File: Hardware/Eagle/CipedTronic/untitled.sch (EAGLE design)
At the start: 14 parts, among them IC1 ATMEGA48/88/168-PU, T1 BC547

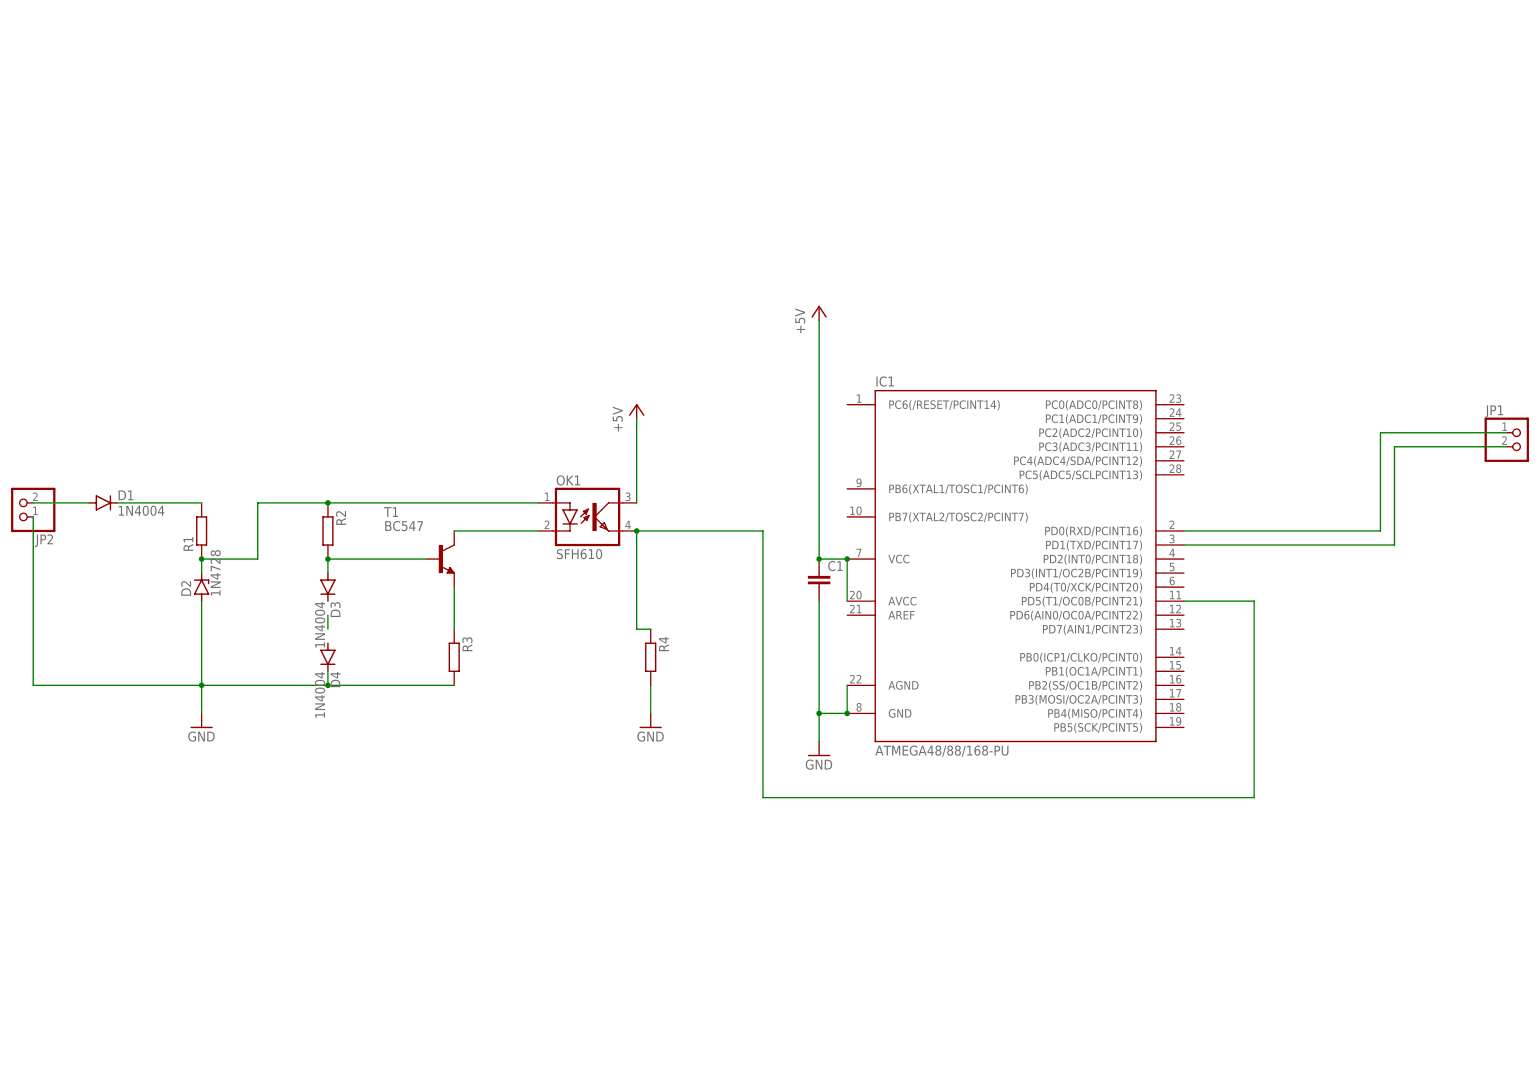
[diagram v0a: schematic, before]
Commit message: migration to seed xaio esp32
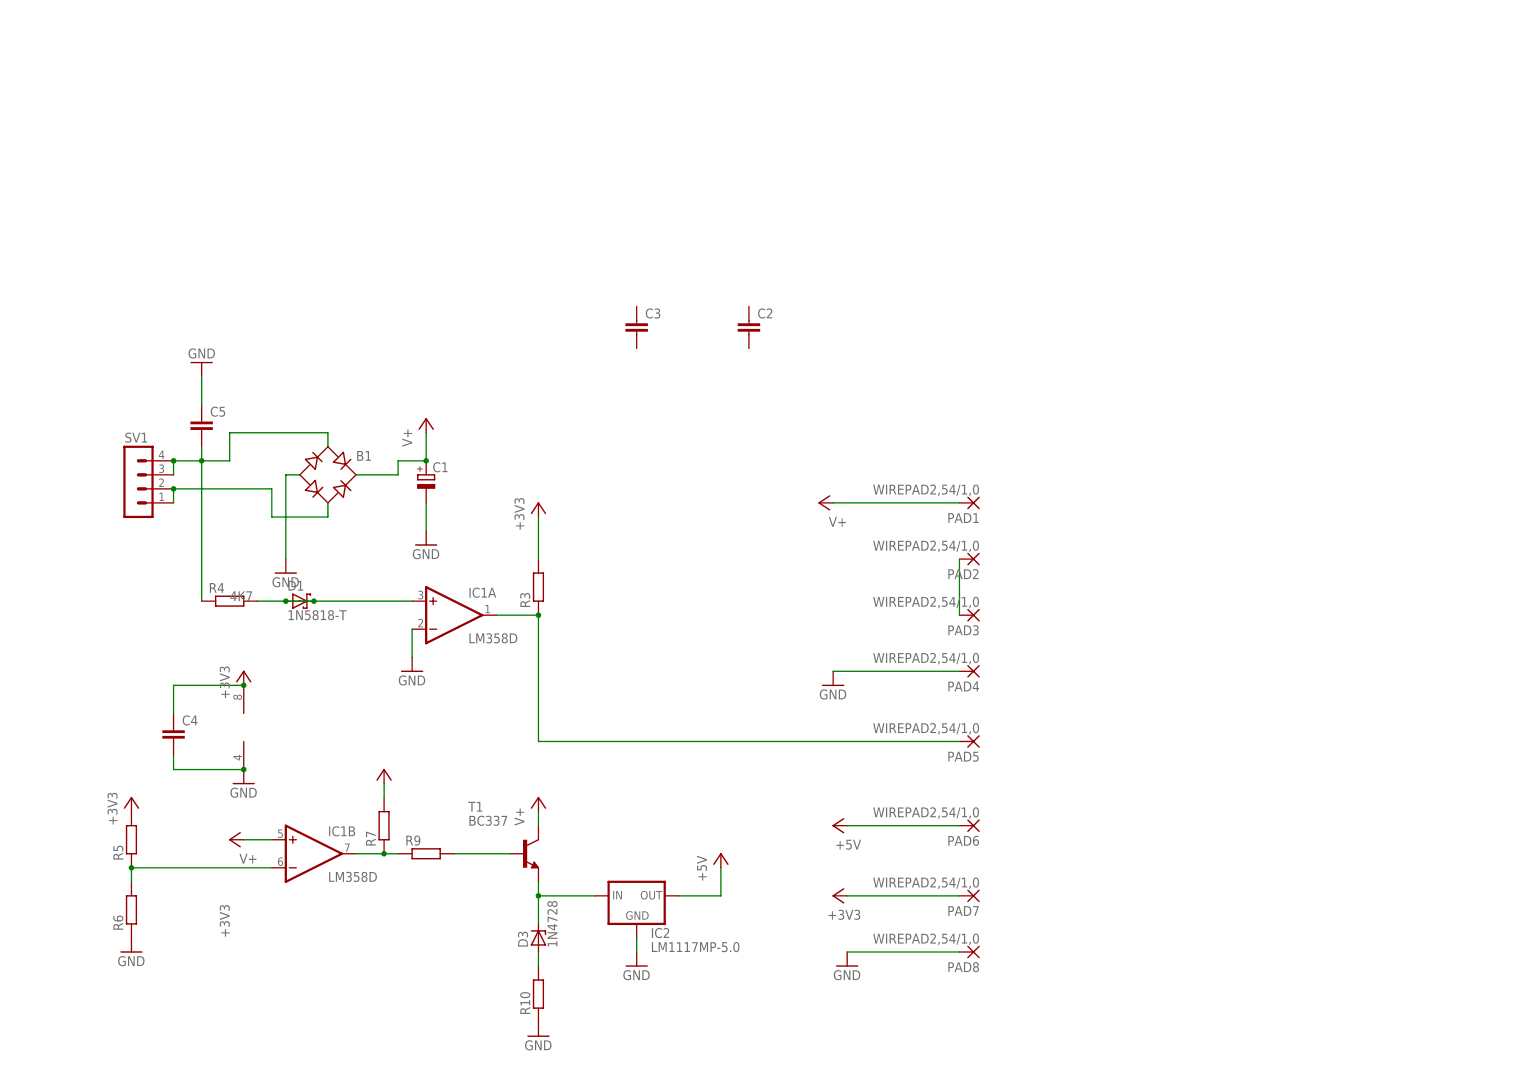
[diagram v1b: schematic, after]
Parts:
- removed D2: 1N4728, diode:1N4728
- removed D4: 1N4004, diode:1N4004
- removed JP1, JP2: (no value), pinhead:PINHD-1X2
- removed OK1: SFH610, optocoupler:SFH610
- removed R1, R2: (no value), rcl:R-EU_0204/7
- added B1: (no value), rectifier:B-DIL
- added C2, C3, C4, C5: (no value), rcl:C-EU050-024X044
- added IC2: LM1117MP-5.0, lm1117_11:LM1117MP-5.0
- added PAD1, PAD2, PAD3, PAD4, PAD5, PAD6, PAD7, PAD8: WIREPAD2,54/1,0, wirepad:WIREPAD2,54/1,0
- added R10, R5, R6, R7, R9: (no value), rcl:R-EU_0204/2V
- added SV1: (no value), con-lstb:MA04-1
- C1: device rcl:C-EU025-024X044 -> rcl:CPOL-EUTT5D11
- D1: value 1N4004 -> 1N5818-T; device diode:1N4004 -> diode:1N5818-T
- D3: value 1N4004 -> 1N4728; device diode:1N4004 -> diode:1N4728
- IC1: value ATMEGA48/88/168-PU -> LM358D; device atmega8:ATMEGA48/88/168-PU -> linear:LM358D
- R3: device rcl:R-EU_0204/7 -> rcl:R-EU_0204/2V
- R4: device rcl:R-EU_0204/7 -> rcl:R-EU_0204/2V; SPICEPREFIX (none) -> 4K7
- T1: value BC547 -> BC337; device transistor:BC547 -> transistor:BC337
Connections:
- removed net N$6: IC1.PD0(RXD/PCINT16), JP1.1
- removed net N$7: OK1.C, T1.C
- new net +3V3: B1.+, C1.+, C4.1, IC1P.V+, PAD7.P, R3.2, R5.2, R7.2
- new net N$11: IC1B.-IN, R5.1, R6.2
- new net N$12: PAD2.P, PAD3.P
- new net N$4: R9.2, T1.B
- new net V+: IC1B.+IN, PAD1.P, T1.C
- net +5V: now also IC2.OUT, PAD6.P; no longer C1.1, IC1.AVCC, IC1.VCC@1, OK1.COL
- net GND: now also B1.-, C1.-, C4.2, C5.1, IC1A.-IN, IC1P.V-, IC2.GND, PAD4.P, PAD8.P, R10.1, R6.1; no longer C1.2, D2.A, D4.C, IC1.AGND, IC1.GND@1, JP2.1, R3.2, R4.2
- net N$1: now also B1.AC1, C5.2, R4.1, SV1.3, SV1.4; no longer D1.C, R1.2
- net N$10: now also D3.A, R10.2; no longer IC1.PD1(TXD/PCINT17), JP1.2
- net N$2: now also B1.AC2, SV1.1, SV1.2; no longer R3.1, T1.E
- net N$3: now also IC1A.OUT, PAD5.P, R3.1; no longer D3.A, R2.2, T1.B
- net N$5: now also D1.A, D1.C, IC1A.+IN, R4.2; no longer D2.C, OK1.A, R1.1, R2.1
- net N$8: now also IC1B.OUT, R7.1, R9.1; no longer D1.A, JP2.2
- net N$9: now also D3.C, IC2.IN, T1.E; no longer IC1.PD5(T1/OC0B/PCINT21), OK1.EMIT, R4.1
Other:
- moved on the sheet: D3, R3, R4, T1

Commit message: Cipedtronic with esp32
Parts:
- added D2: 1N4728, diode:1N4728
- added D4, D5: 1N5818-T, diode:1N5818-T
- added R1, R8: 10k, rcl:R-EU_0204/2V
- added R2: 1m, rcl:R-EU_0204/2V
- C2: value (none) -> 0,1uf
- C3: value (none) -> 0.33uf
- R3: value (none) -> 10k
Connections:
- net N$2 renamed V-
- new net N$6: IC1A.+IN, R1.1, R2.2
- new net N$7: D4.A, D4.C, D5.A, IC1A.-IN, R3.2
- net +3V3: now also R3.1, R8.1; no longer R3.2
- net +5V: now also C2.1
- net GND: now also C2.2, C3.2, D2.A, D5.C; no longer IC1A.-IN
- net N$3: now also R2.1, R8.2; no longer R3.1
- net N$5: now also D2.C, R1.2; no longer IC1A.+IN
- net N$9: now also C3.1
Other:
- moved on the sheet: C2, C3, R3

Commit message: Rename sketch Extend Timer Add namespace
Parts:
- removed C1: (no value), rcl:CPOL-EUTT5D11
- removed D3: 1N4728, diode:1N4728
- removed R10, R9: (no value), rcl:R-EU_0204/2V
- removed T1: BC337, transistor:BC337
- added PAD10, PAD9: Light on/off switch, wirepad:2,15/1,0
- added Q1, Q3: FDD4141TO252, transistor-fet:FDD4141TO252
- PAD1: value WIREPAD2,54/1,0 -> Light on/off ESP32; device wirepad:WIREPAD2,54/1,0 -> wirepad:2,15/1,0
- PAD2: value WIREPAD2,54/1,0 -> 5V ESP32; device wirepad:WIREPAD2,54/1,0 -> wirepad:2,15/1,0
- PAD3: value WIREPAD2,54/1,0 -> 3.3V ESP32; device wirepad:WIREPAD2,54/1,0 -> wirepad:2,15/1,0
- PAD4, PAD5: value WIREPAD2,54/1,0 -> LED; device wirepad:WIREPAD2,54/1,0 -> wirepad:2,15/1,0
- PAD6: value WIREPAD2,54/1,0 -> Pulses ESP32; device wirepad:WIREPAD2,54/1,0 -> wirepad:2,15/1,0
- PAD7, PAD8: value WIREPAD2,54/1,0 -> Super Cap; device wirepad:WIREPAD2,54/1,0 -> wirepad:2,15/1,0
- R5: value (none) -> 10k; device rcl:R-EU_0204/2V -> rcl:R-EU_MELF0204W
- R6, R7: value (none) -> 10k
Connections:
- removed net N$10: D3.A, R10.2
- removed net N$11: IC1B.-IN, R5.1, R6.2
- removed net N$12: PAD2.P, PAD3.P
- new net N$13: D1.A, R4.2
- new net N$2: PAD4.P, Q3.D
- net +3V3: now also PAD10.P, PAD2.P; no longer C1.+, R5.2, R7.2
- net +5V: now also PAD3.P; no longer PAD6.P
- net GND: now also PAD5.P, R5.2, R7.2; no longer C1.-, PAD4.P, R10.1, R6.1
- net N$3: now also PAD6.P; no longer PAD5.P
- net N$4: now also C3.1, IC2.IN, Q1.D; no longer R9.2, T1.B
- net N$5: no longer D1.A, R4.2
- net N$8: now also PAD1.P, PAD9.P, Q3.G; no longer IC1B.OUT, R9.1
- net N$9: now also Q1.G, R5.1, R6.2; no longer C3.1, D3.C, IC2.IN, T1.E
- net V+: now also Q1.S, Q3.S, R6.1; no longer IC1B.+IN, PAD1.P, T1.C
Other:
- note added: "10K"
- note added: "3.3 V"
- note added: "Reference 1 Volt"
- note added: "Should switch >= 5Volts"
- moved on the sheet: C2, C3, C4, D1, D2, D4, D5, IC1A, IC2, R1, R2, R3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

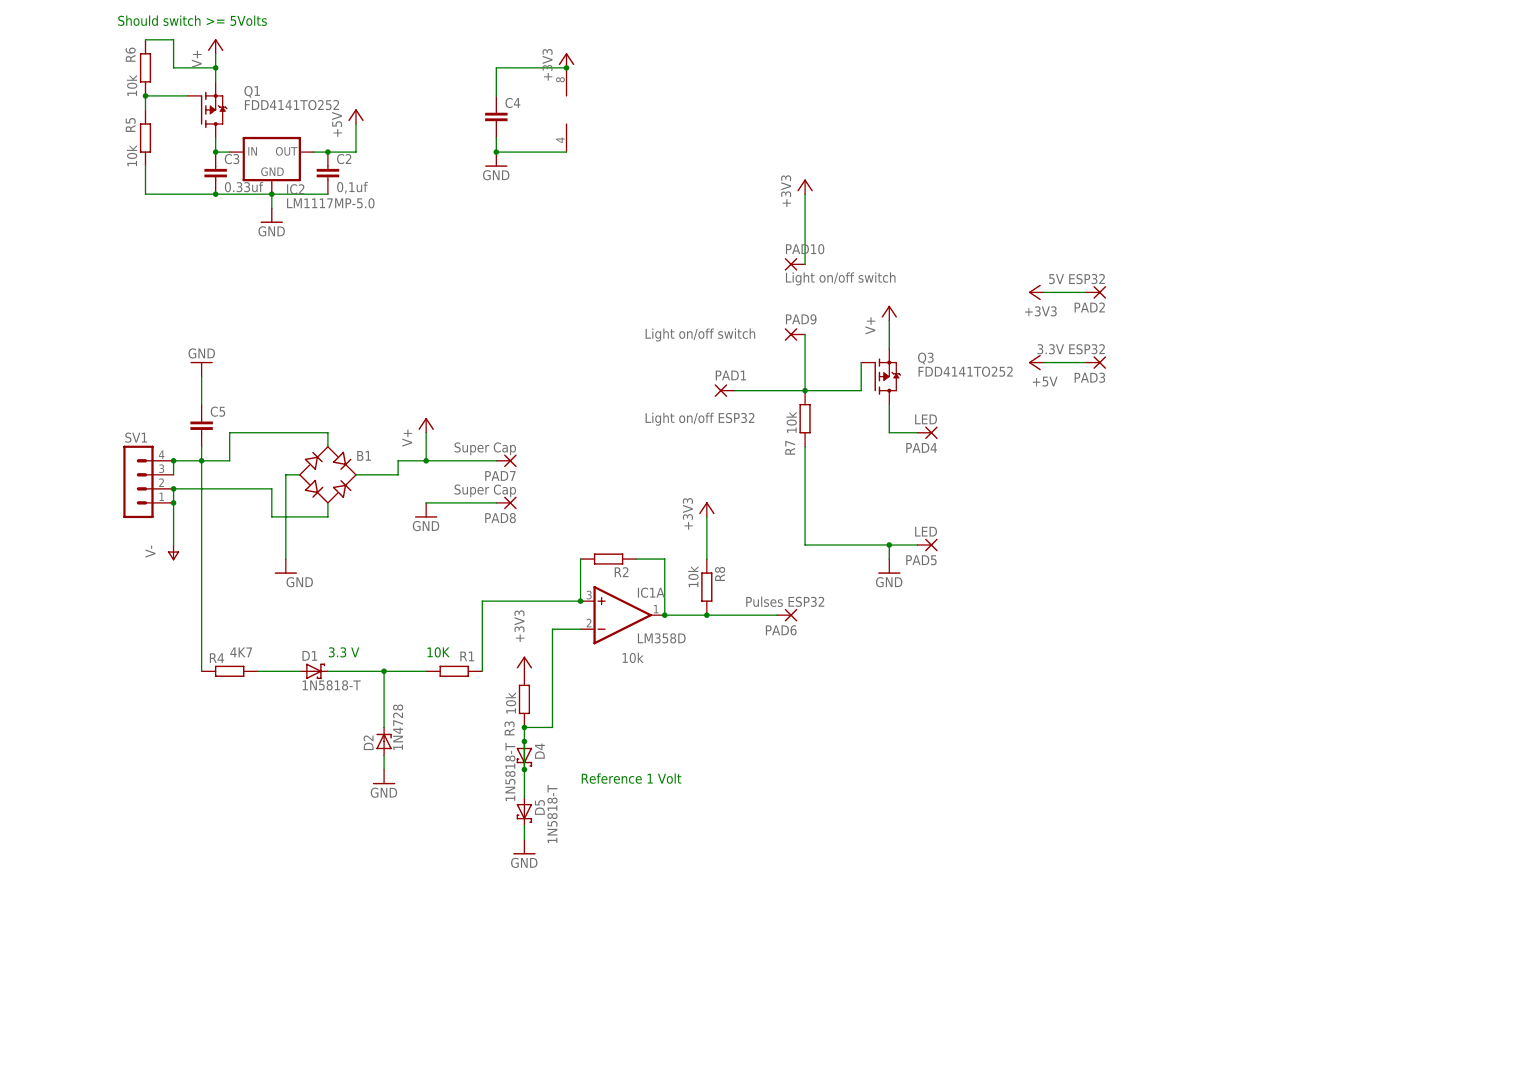
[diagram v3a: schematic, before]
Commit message: battery load functions distance sensor improved pulse formatting
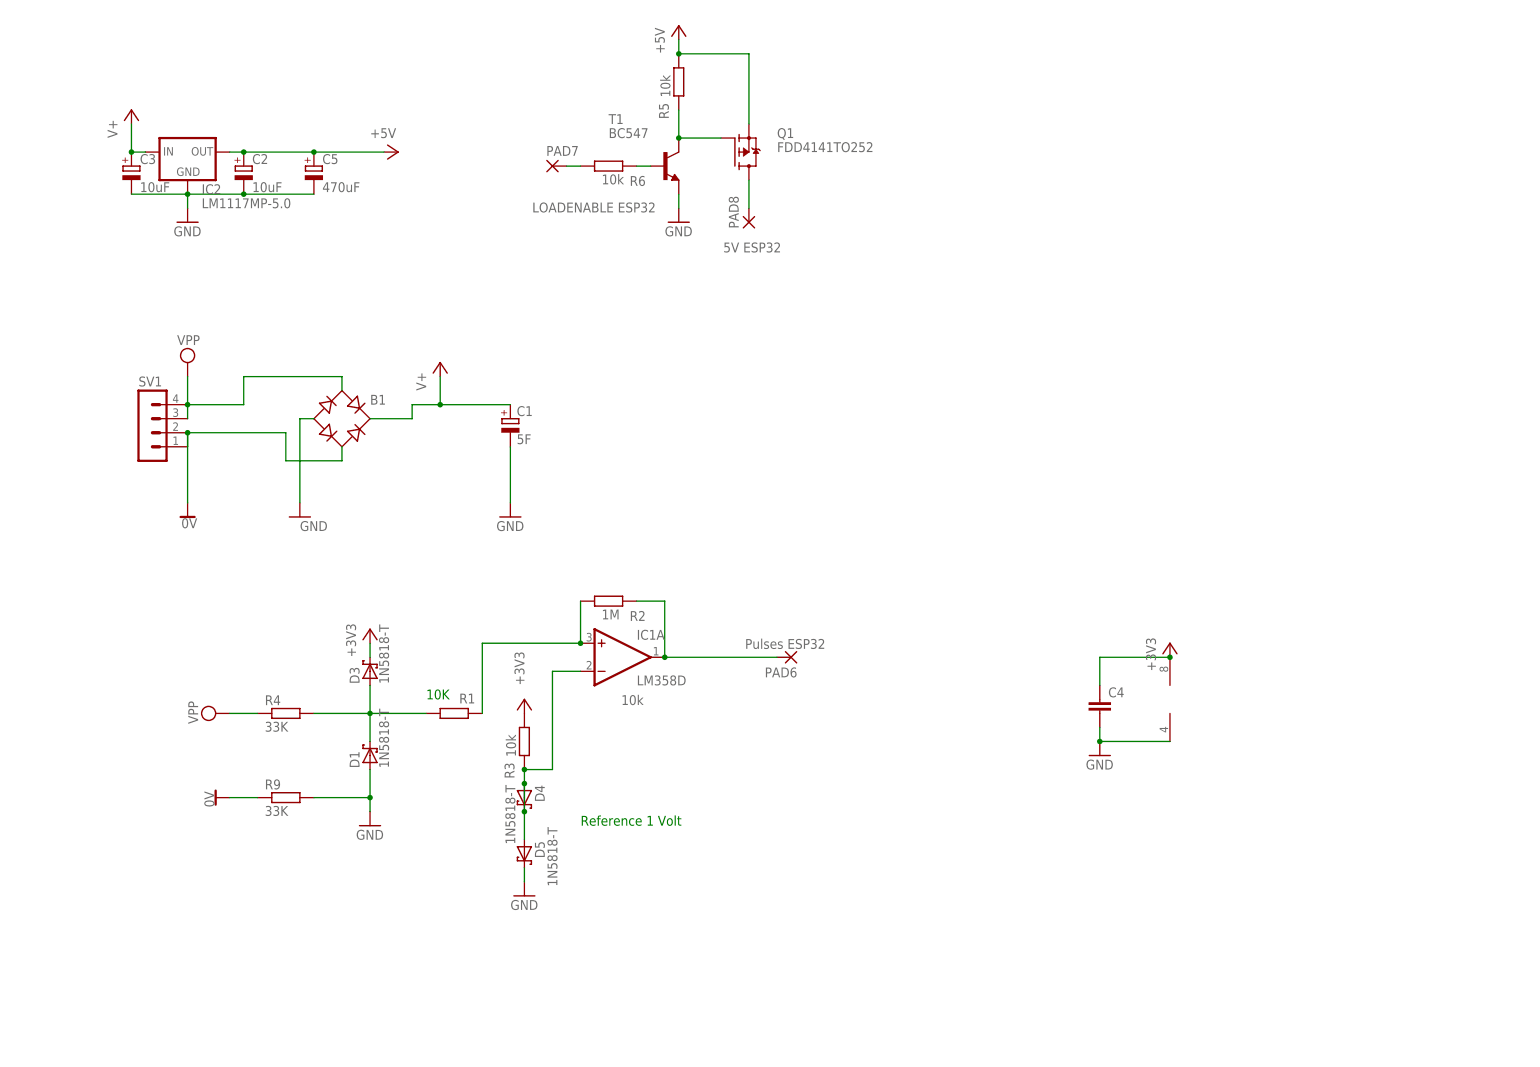
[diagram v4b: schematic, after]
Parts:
- removed D2: 1N4728, diode:1N4728
- removed PAD1: Light on/off ESP32, wirepad:2,15/1,0
- removed PAD10, PAD9: Light on/off switch, wirepad:2,15/1,0
- removed PAD2: 5V ESP32, wirepad:2,15/1,0
- removed PAD3: 3.3V ESP32, wirepad:2,15/1,0
- removed PAD4, PAD5: LED, wirepad:2,15/1,0
- removed Q3: FDD4141TO252, transistor-fet:FDD4141TO252
- removed R7, R8: 10k, rcl:R-EU_0204/2V
- added C1: 5F, rcl:CPOL-EUE2,5-6E
- added D3: 1N5818-T, diode:1N5818-T
- added R9: 33K, rcl:R-EU_0204/2V
- added T1: BC547, transistor:BC547
- C2: value 0,1uf -> 10uF; device rcl:C-EU050-024X044 -> rcl:CPOL-EUE2,5-6E
- C3: value 0.33uf -> 10uF; device rcl:C-EU050-024X044 -> rcl:CPOL-EUE2,5-6E
- C5: value (none) -> 470uF; device rcl:C-EU050-024X044 -> rcl:CPOL-EUE2,5-6E
- PAD7: value Super Cap -> LOADENABLE ESP32
- PAD8: value Super Cap -> 5V ESP32
- R2: value 1m -> 1M
- R4: value (none) -> 33K
- R5: device rcl:R-EU_MELF0204W -> rcl:R-EU_0204/2V
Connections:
- removed net N$1: B1.AC1, C5.2, R4.1, SV1.3, SV1.4
- removed net N$13: D1.A, R4.2
- removed net N$2: PAD4.P, Q3.D
- removed net N$8: PAD1.P, PAD9.P, Q3.G, R7.1
- removed net V-: B1.AC2, SV1.1, SV1.2
- new net 0V: B1.AC2, R9.1, SV1.1, SV1.2
- new net N$10: PAD8.P, Q1.D
- new net N$11: D1.C, D3.A, R1.2, R4.2
- new net VPP: B1.AC1, R4.1, SV1.3, SV1.4
- net +3V3: now also C1.+, D3.C; no longer PAD10.P, PAD2.P, PAD7.P, R8.1
- net +5V: now also C2.+, C5.+, Q1.S, R5.1; no longer C2.1, PAD3.P
- net GND: now also C1.-, C2.-, C3.-, C5.-, D1.A, R9.2, T1.E; no longer C2.2, C3.2, C5.1, D2.A, PAD5.P, PAD8.P, R5.2, R7.2
- net N$3: now also R2.2; no longer R2.1, R8.2
- net N$4: now also PAD7.P, R6.1; no longer C3.1, IC2.IN, Q1.D
- net N$5: now also R6.2, T1.B; no longer D1.C, D2.C, R1.2
- net N$6: now also R2.1; no longer R2.2
- net N$9: now also R5.2, T1.C; no longer R5.1, R6.2
- net V+: now also C3.+, IC2.IN; no longer Q1.S, Q3.S, R6.1
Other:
- note removed: "3.3 V"
- note removed: "Should switch >= 5Volts"
- moved on the sheet: B1, C4, D1, D4, D5, IC1A, IC2, PAD6, PAD7, PAD8, Q1, R1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
